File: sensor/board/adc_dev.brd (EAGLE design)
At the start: 160 x 100 mm, 6 parts, among them U1 FT232RL-BASICSSOP

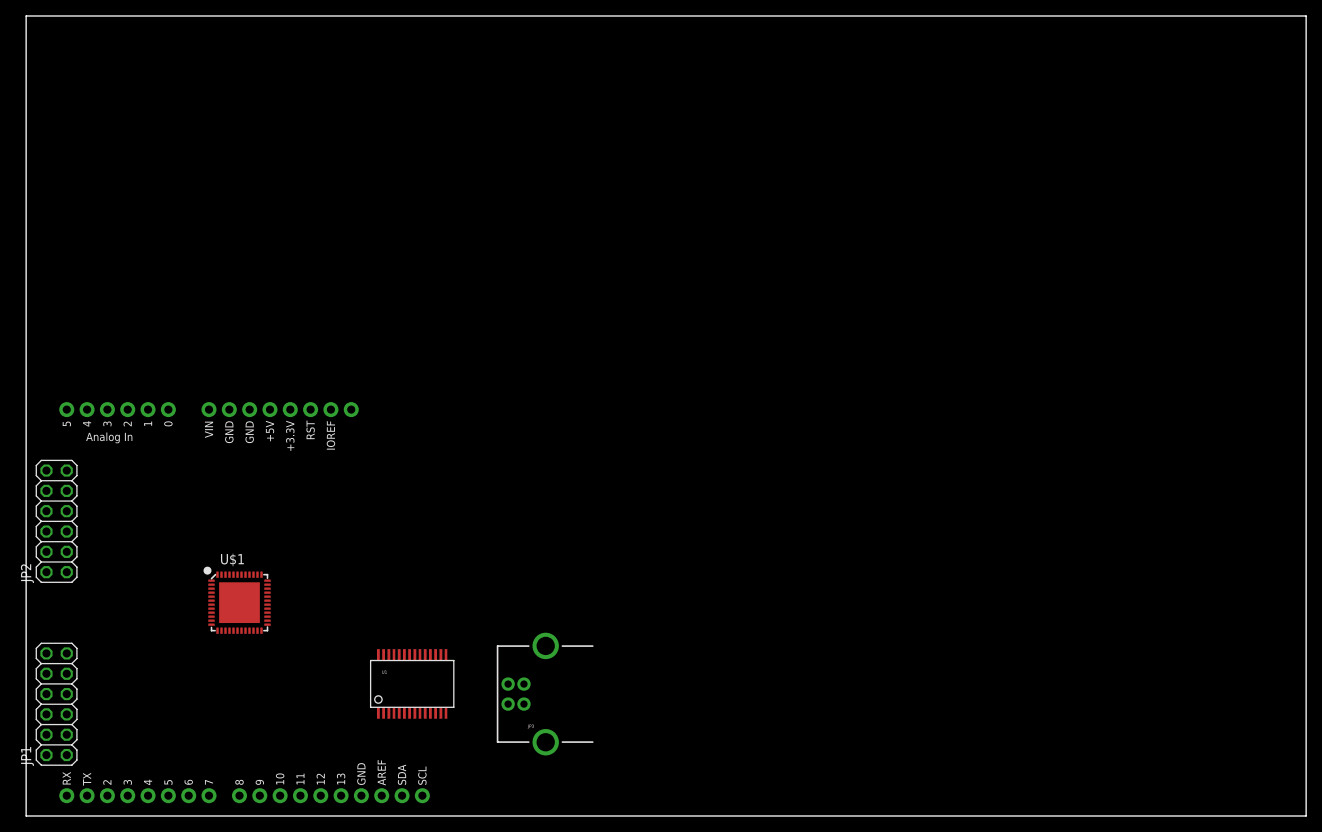
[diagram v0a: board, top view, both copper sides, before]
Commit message: Schematic pretty much done, need to pinswap before layout
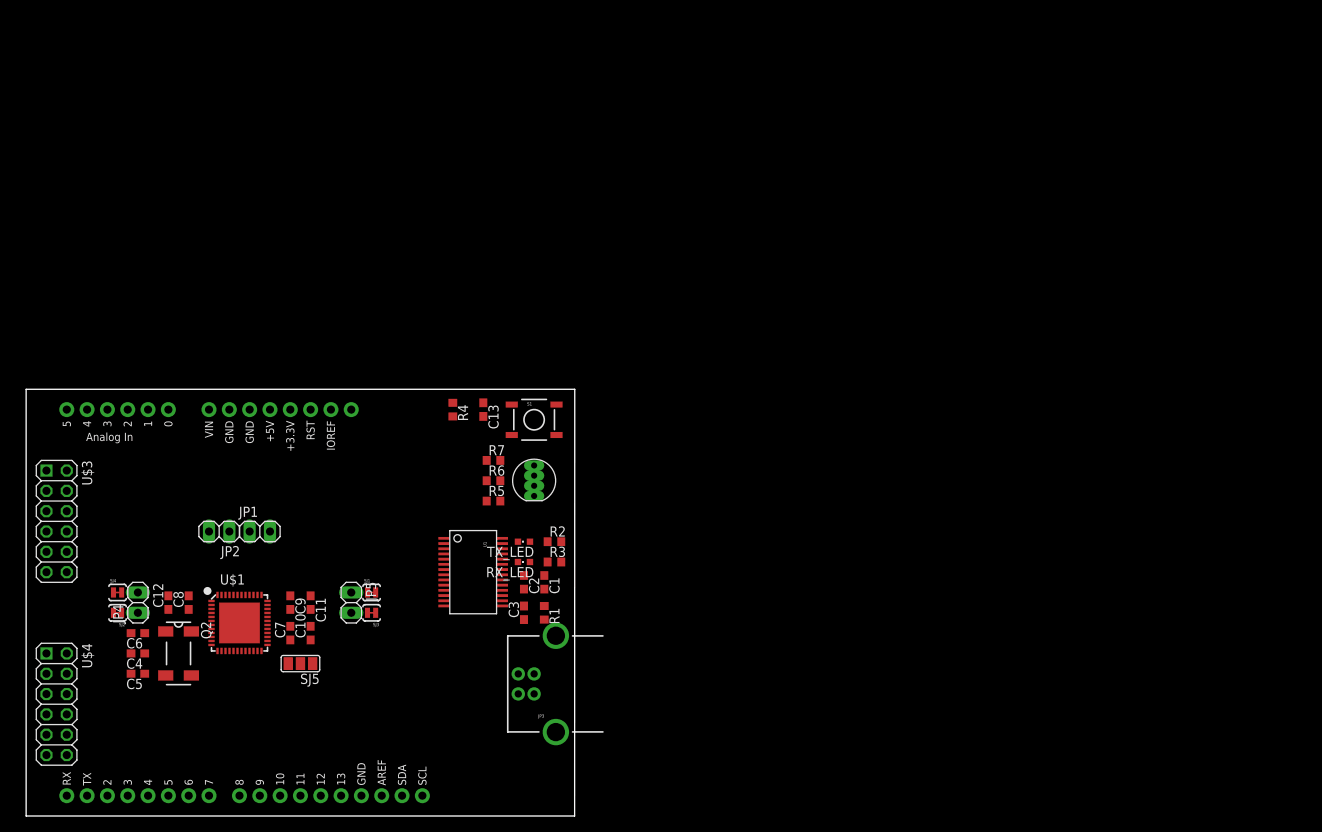
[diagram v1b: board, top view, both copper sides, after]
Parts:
- added C1, C13, C3, C7, C8, C9: 100nF, rcl:C0603
- added C10, C11, C12, C2: 10uF, rcl:C0603
- added C4, C5: 4.7pF, rcl:C0603
- added C6: 22nF, rcl:C0603
- added D1: LED-RGB-CA-THRUCLEAR, SparkFun-LED:LED-RGB-THRU
- added JP4, JP5: (no value), pinhead:1X02
- added Q2: MC-306 32.7680K-A0, crystal:MC-306
- added R1: FERRITE, rcl:R0603
- added R2, R5: 120R, rcl:R0603
- added R3: 68R, rcl:R0603
- added R4: 10k, rcl:R0603
- added R6, R7: 10R, rcl:R0603
- added RX_LED, TX_LED: (no value), led:CHIPLED_0603
- added S1: TAC_SWITCHSMD, SparkFun-Electromechanical:TACTILE-SWITCH-SMD
- added SJ1, SJ2, SJ3, SJ4: JUMPER-PAD-2-NC_BY_TRACE, SparkFun-Passives:PAD-JUMPER-2-NC_BY_TRACE_YES_SILK
- added SJ5: JUMPER-PAD-3-NOFULL_BOX_SILK, SparkFun-Passives:PAD-JUMPER-3-NO_YES_SILK_FULL_BOX
- added U$3, U$4: PMOD, modular_robotics:2X06
- JP1, JP2: device pinhead:2X06 -> pinhead:1X02
- moved JP1 33.3 mm to (29.2, 35.6), turned to 0 degrees
- moved JP2 20.4 mm to (24.1, 35.6), turned to 180 degrees
- moved U1 15.9 mm to (55.9, 30.5), turned to 270 degrees
- moved U$1 2.54 mm to (26.7, 24.1)
- moved JP3 1.80 mm to (63.5, 16.5)
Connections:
- removed net GND1: U1.7
- removed net GND2: U1.18
- removed net GND3: U1.21
- removed net VCC: U1.20
- removed net VCCIO: U1.4
- new net +3V3: C10.1, C7.1, D1.2, R2.2, R3.2, R4.2, SJ1.2, SJ2.2, SJ5.1, U$1.10, U$1.28, U$2.3.3V, U$2.IOREF, U$3.11, U$3.12, U$4.11, U$4.12, U1.4
- new net +5V: C1.1, C2.1, R1.1, U$2.5V, U1.20
- new net A0: U$1.20, U$1.4, U$2.A0
- new net A1: U$1.21, U$1.3, U$2.A1
- new net A2: U$1.2, U$2.A2
- new net A3: U$1.1, U$2.A3
- new net A4: U$1.48, U$2.A4
- new net A5: U$1.47, U$2.A5
- new net D10: R6.1, U$1.34, U$2.D10, U$4.6
- new net D11: R7.1, U$1.33, U$2.D11, U$4.8
- new net D12: U$1.16, U$2.D12
- new net D13: U$1.17, U$2.D13
- new net D2: U$1.18, U$1.46, U$2.D2
- new net D3: U$1.45, U$2.D3, U$4.3
- new net D4: U$1.19, U$1.40, U$2.D4
- new net D5: U$1.39, U$2.D5, U$4.7
- new net D6: U$1.38, U$2.D6, U$4.2
- new net D7: U$1.14, U$1.37, U$2.D7
- new net D8: U$1.15, U$1.36, U$2.D8
- new net D9: R5.1, U$1.35, U$2.D9, U$4.4
- new net DRDY: U$1.25, U$4.5
- new net GND: C1.2, C10.2, C13.2, C2.2, C3.2, C7.2, JP3.GND, S1.3, S1.4, SJ3.1, SJ4.1, SJ5.3, U$1.12, U$1.29, U$2.GND@0, U$2.GND@1, U$2.GND@2, U$3.10, U$3.9, U$4.10, U$4.9, U1.18, U1.21, U1.25, U1.26, U1.7
- new net MISO: U$1.24, U$3.5
- new net MOSI: U$1.23, U$3.3
- new net N$1: JP3.D+, U1.15
- new net N$10: JP1.1, U$1.42
- new net N$11: C12.1, C8.1, JP4.1, SJ2.1, U$1.6
- new net N$12: C11.2, C9.2, JP5.2, SJ3.2, U$1.30
- new net N$13: C6.1, U$1.7
- new net N$14: C4.1, Q2.4, U$1.8
- new net N$15: C5.1, Q2.1, U$1.9
- new net N$16: JP1.2, U$1.41
- new net N$17: D1.1, R5.2
- new net N$18: D1.3, R6.2
- new net N$19: JP2.2, U$1.44
- new net N$2: JP3.D-, U1.16
- new net N$20: JP2.1, U$1.43
- new net N$21: D1.4, R7.2
- new net N$3: R2.1, TX_LED.A
- new net N$4: R3.1, RX_LED.A
- new net N$5: C3.1, U1.17
- new net N$6: SJ5.2, U$1.26
- new net N$7: JP3.VBUS, R1.2
- new net N$8: TX_LED.C, U1.23
- new net N$9: RX_LED.C, U1.22
- new net RESET: C13.1, R4.1, S1.1, S1.2, U$1.11, U$2.RES, U$4.1
- new net RX: U$2.RX, U$3.2, U1.5
- new net SCK: U$1.22, U$3.7
- new net SCL: U$2.SCL, U$3.8
- new net SDA: U$2.SDA, U$3.6
- new net SS: U$1.27, U$3.1
- new net TX: U$2.TX, U$3.4, U1.1
- new net VREFP: C11.1, C9.1, JP5.1, SJ1.1, U$1.31, U$2.AREF
- net AGND: now also C12.2, C4.2, C5.2, C6.2, C8.2, JP4.2, SJ4.2, U$1.32, U$1.5; no longer U1.25
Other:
- board size 160 x 100 mm -> 68.6 x 53.3 mm

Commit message: Rough layout getting there
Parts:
- added R8, R9: 4k7, rcl:R0603
- S1: device SparkFun-Electromechanical:TACTILE-SWITCH-SMD -> SparkFun-Electromechanical:TACTILE_SWITCH_SMD
- SJ5: value JUMPER-PAD-3-NOFULL_BOX_SILK -> JUMPER-PAD-3-NOYES_SILK; device SparkFun-Passives:PAD-JUMPER-3-NO_YES_SILK_FULL_BOX -> SparkFun-Passives:PAD-JUMPER-3-NO_YES_SILK
- moved SJ3 23.2 mm to (24.7, 11.3), turned to 90 degrees
- moved SJ1 23.0 mm to (27.3, 11.3), turned to 270 degrees
- moved U$3 22.9 mm to (3.81, 14.0)
- moved U$4 22.9 mm to (3.81, 36.8)
- moved SJ4 22.5 mm to (28.4, 42.7), turned to 270 degrees
- moved SJ2 22.4 mm to (25.7, 42.7), turned to 90 degrees
- moved JP5 19.4 mm to (26.0, 14.0), turned to 180 degrees
- moved JP4 18.7 mm to (27.0, 40.1), turned to 0 degrees
- moved C6 18.7 mm to (26.1, 37.1), turned to 0 degrees
- moved C5 17.5 mm to (19.1, 34.5), turned to 90 degrees
- moved C4 17.4 mm to (24.0, 34.5), turned to 90 degrees
- moved SJ5 14.8 mm to (19.5, 18.0), turned to 270 degrees
- moved Q2 14.4 mm to (21.5, 34.5), turned to 90 degrees
- moved C10 14.3 mm to (22.5, 17.0), turned to 0 degrees
- moved JP1 14.2 mm to (33.5, 22.0), turned to 270 degrees
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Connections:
- net +3V3: now also R8.2, R9.2
- net A0: now also U$1.15, U$1.47; no longer U$1.20, U$1.4
- net A1: now also U$1.14, U$1.48; no longer U$1.21, U$1.3
- net A2: now also U$1.1; no longer U$1.2
- net A3: now also U$1.2; no longer U$1.1
- net A4: now also U$1.3; no longer U$1.48
- net A5: now also U$1.4; no longer U$1.47
- net AGND: now also U$1.EPAD
- net D10: now also U$4.4; no longer U$4.6
- net D11: now also U$4.2; no longer U$4.8
- net D12: now also U$1.21; no longer U$1.16
- net D13: now also U$1.19; no longer U$1.17
- net D2: now also U$1.16; no longer U$1.18
- net D3: now also U$1.37, U$4.7; no longer U$1.45, U$4.3
- net D4: now also U$1.17, U$1.45; no longer U$1.19, U$1.40
- net D5: now also U$1.36, U$4.8; no longer U$1.39, U$4.7
- net D6: now also U$4.3; no longer U$4.2
- net D7: now also U$1.18, U$1.40; no longer U$1.14, U$1.37
- net D8: now also U$1.20, U$1.39; no longer U$1.15, U$1.36
- net D9: now also U$4.6; no longer U$4.4
- net MISO: now also U$3.6; no longer U$3.5
- net MOSI: now also U$3.4; no longer U$3.3
- net N$14: now also Q2.1; no longer Q2.4
- net N$15: now also Q2.4; no longer Q2.1
- net RX: now also U$3.1; no longer U$3.2
- net SCK: now also U$3.2; no longer U$3.7
- net SCL: now also R9.1, U$3.7; no longer U$3.8
- net SDA: now also R8.1, U$3.5; no longer U$3.6
- net SS: now also U$3.8; no longer U$3.1
- net TX: now also U$3.3; no longer U$3.4
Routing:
- net +3V3: track 0.00 -> 159.2 mm, vias 0 -> 3
- net D11: track 0.00 -> 79.4 mm, vias 0 -> 4
- net D10: track 0.00 -> 76.0 mm, vias 0 -> 4
- net D9: track 0.00 -> 70.7 mm, vias 0 -> 4
- net A0: track 0.00 -> 68.7 mm, vias 0 -> 1
- net D6: track 0.00 -> 66.2 mm, vias 0 -> 2
- net A1: track 0.00 -> 63.2 mm, vias 0 -> 1
- net D3: track 0.00 -> 60.9 mm, vias 0 -> 2
- net SCL: track 0.00 -> 60.0 mm, vias 0 -> 1
- net SDA: track 0.00 -> 58.9 mm, vias 0 -> 1
- net D5: track 0.00 -> 58.4 mm, vias 0 -> 2
- net RESET: track 0.00 -> 54.5 mm, vias 0 -> 1
- net D2: track 0.00 -> 51.5 mm, vias 0 -> 3
- net D7: track 0.00 -> 47.0 mm, vias 0 -> 2
- net D13: track 0.00 -> 47.0 mm, vias 0 -> 2
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- added copper zone on layer 1, net GND
- added copper zone on layer 16, net GND

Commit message: ADC layout mostly done, just need to finish bonus parts
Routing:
- net RX: track 20.2 -> 66.6 mm
- net TX: track 19.5 -> 63.2 mm
- net D11: track 79.4 -> 84.1 mm
- net D10: track 76.0 -> 80.1 mm
- net D9: track 70.7 -> 74.1 mm
- net D8: track 37.7 -> 34.8 mm
- net D5: track 58.4 -> 61.1 mm
- net D3: track 60.9 -> 58.5 mm
- net D12: track 42.0 -> 44.3 mm
- net D6: track 66.2 -> 68.3 mm
- net D13: track 47.0 -> 49.1 mm
- net D7: track 47.0 -> 45.2 mm
- net D4: track 46.8 -> 48.2 mm
- net SCL: track 60.0 -> 59.3 mm

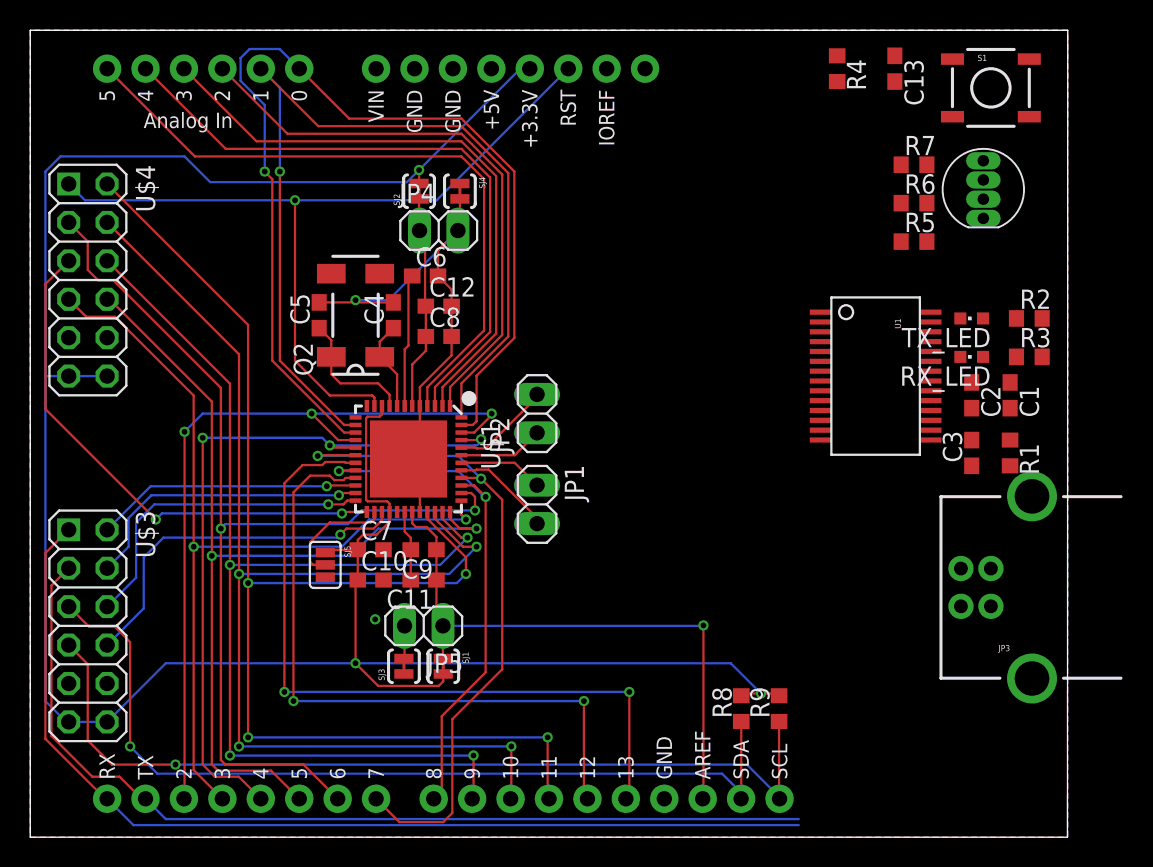
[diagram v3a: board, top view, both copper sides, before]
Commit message: Layout pretty much done, need to clean up schematic and do silkscreen
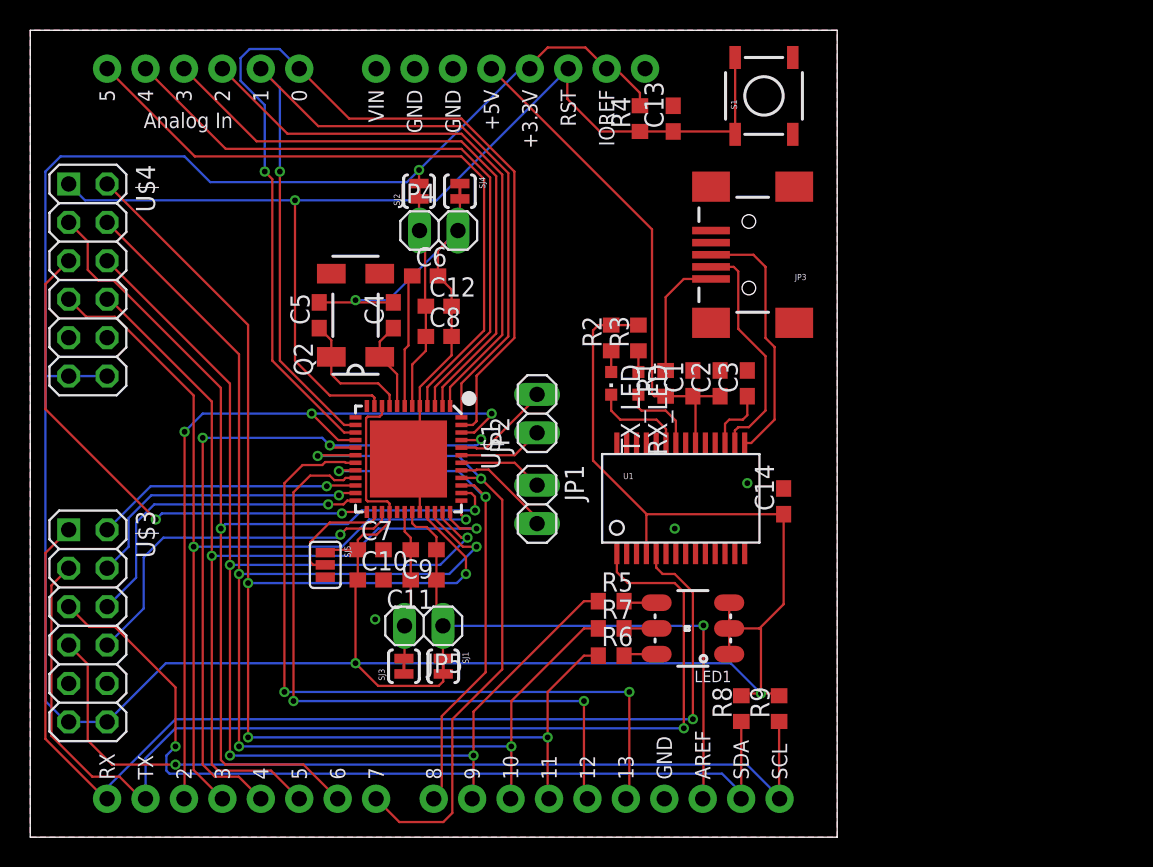
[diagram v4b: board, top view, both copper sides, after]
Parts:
- removed D1: LED-RGB-CA-THRUCLEAR, SparkFun-LED:LED-RGB-THRU
- added C14: 100nF, rcl:C0603
- added LED1: LED-TRICOLOR-5050NO_IC, SparkFun-LED:LED-TRICOLOR-5050
- JP3: value USB-B -> USBSMD; device SparkFun-Connectors:USB-B-PTH -> SparkFun-Connectors:USB-MINIB
- R5: value 120R -> 10R
- R7: value 10R -> 68R
- moved R7 36.6 mm to (38.4, 13.8)
- moved R6 36.0 mm to (38.4, 12.0)
- moved R5 31.1 mm to (38.4, 15.6)
- moved R2 27.7 mm to (38.4, 33.0), turned to 90 degrees
- moved JP3 27.2 mm to (47.5, 38.5)
- moved R3 25.9 mm to (40.2, 33.0), turned to 90 degrees
- moved TX_LED 24.2 mm to (38.4, 30.0), turned to 180 degrees
- moved R1 23.2 mm to (42.0, 30.0), turned to 90 degrees
- moved RX_LED 22.1 mm to (40.2, 30.0), turned to 180 degrees
- moved C1 21.0 mm to (43.8, 30.0), turned to 90 degrees
- moved C2 16.6 mm to (45.6, 30.0), turned to 90 degrees
- moved C3 15.5 mm to (47.4, 30.0)
- moved U1 15.2 mm to (43.0, 22.4), turned to 0 degrees
- moved C13 15.0 mm to (42.5, 47.5), turned to 90 degrees
- moved S1 15.0 mm to (48.5, 49.0), turned to 90 degrees
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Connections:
- net +3V3: now also C14.1, LED1.1, LED1.2, LED1.3; no longer D1.2
- net D10: now also R7.1; no longer R6.1
- net D11: now also R6.1; no longer R7.1
- net GND: now also C14.2
- net N$17: now also LED1.4; no longer D1.1
- net N$18: now also LED1.6; no longer D1.3
- net N$21: now also LED1.5; no longer D1.4
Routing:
- net +3V3: track 159.2 -> 215.8 mm
- net +5V: track 0.00 -> 33.6 mm
- net RESET: track 54.5 -> 73.7 mm
- net N$1: track 0.00 -> 16.9 mm
- net N$2: track 0.00 -> 15.3 mm
- net D9: track 74.1 -> 88.3 mm
- net D10: track 80.1 -> 90.9 mm
- net TX: track 63.2 -> 73.8 mm, vias 0 -> 1
- net N$7: track 0.00 -> 8.35 mm
- net D11: track 84.1 -> 91.5 mm
- net RX: track 66.6 -> 73.9 mm, vias 0 -> 1
- net N$8: track 0.00 -> 6.10 mm
- net N$9: track 0.00 -> 5.16 mm
- net N$5: track 0.00 -> 4.23 mm
- net N$18: track 0.00 -> 2.19 mm
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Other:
- board size 68.6 x 53.3 mm -> 53.3 x 53.3 mm

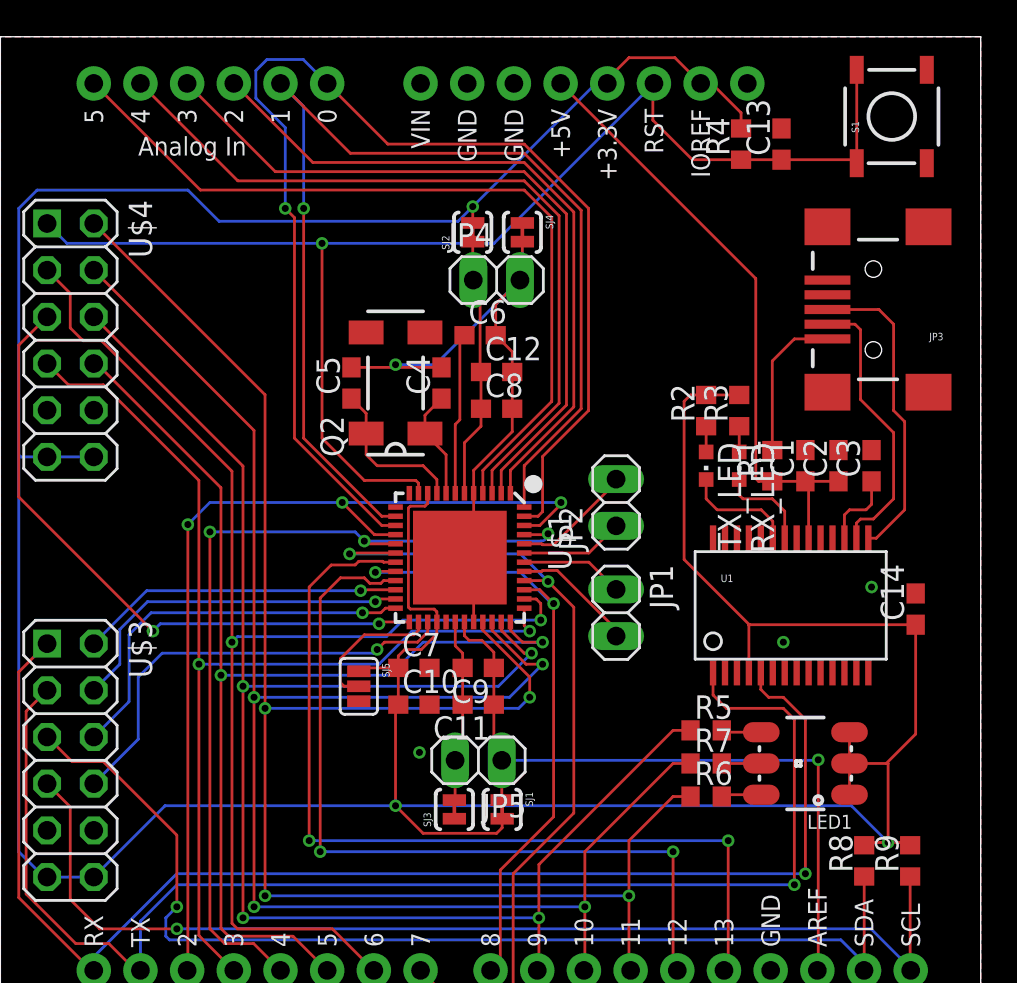
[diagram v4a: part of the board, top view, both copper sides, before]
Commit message: Tweak capacitor, made BLDC + ADC panel.
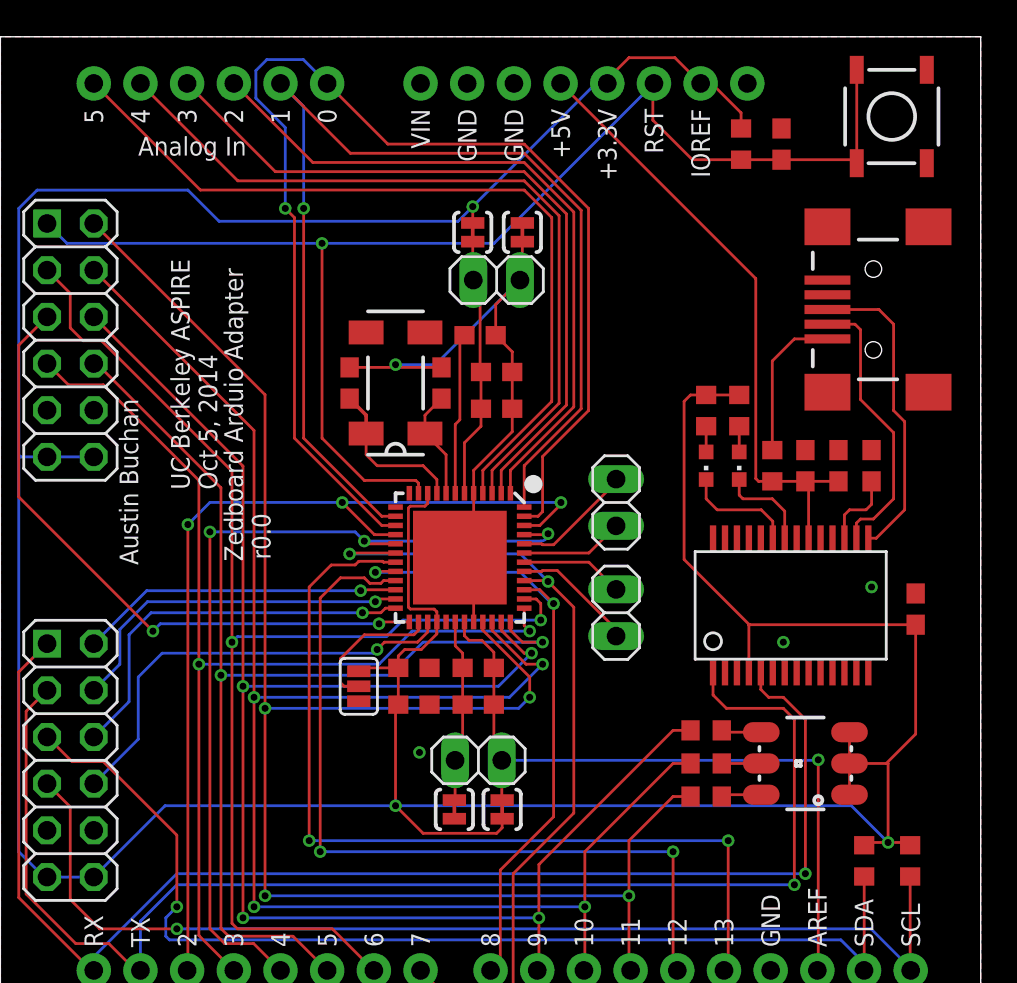
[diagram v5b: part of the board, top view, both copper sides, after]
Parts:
- added U$5: INFO, modular_robotics:INFO
- U1: value FT232RL-BASICSSOP -> FT232RL
- moved C5 0.10 mm to (19.0, 34.5)
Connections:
- net N$10 renamed ADCP
- net N$11 renamed AVDD
- net N$12 renamed VREFN
- net N$16 renamed ADCN
- net N$19 renamed MUXP
- net N$20 renamed MUXN
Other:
- board text added: "ADCN"
- board text added: "ADCP"
- board text added: "AGND"
- board text added: "AVDD"
- board text added: "MUXN"
- board text added: "MUXP"
- board text added: "REFN"
- board text added: "REFP"
- board text added: "austin.d.buchan@gmail.com"
